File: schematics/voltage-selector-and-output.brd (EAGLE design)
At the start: 55.5 x 41.9 mm, 31 parts, among them IC1 5V, IC2 MIC2941, IC3 MCP41010P, IC5 12V, IC6 ATTINY85, Q1 2N3906

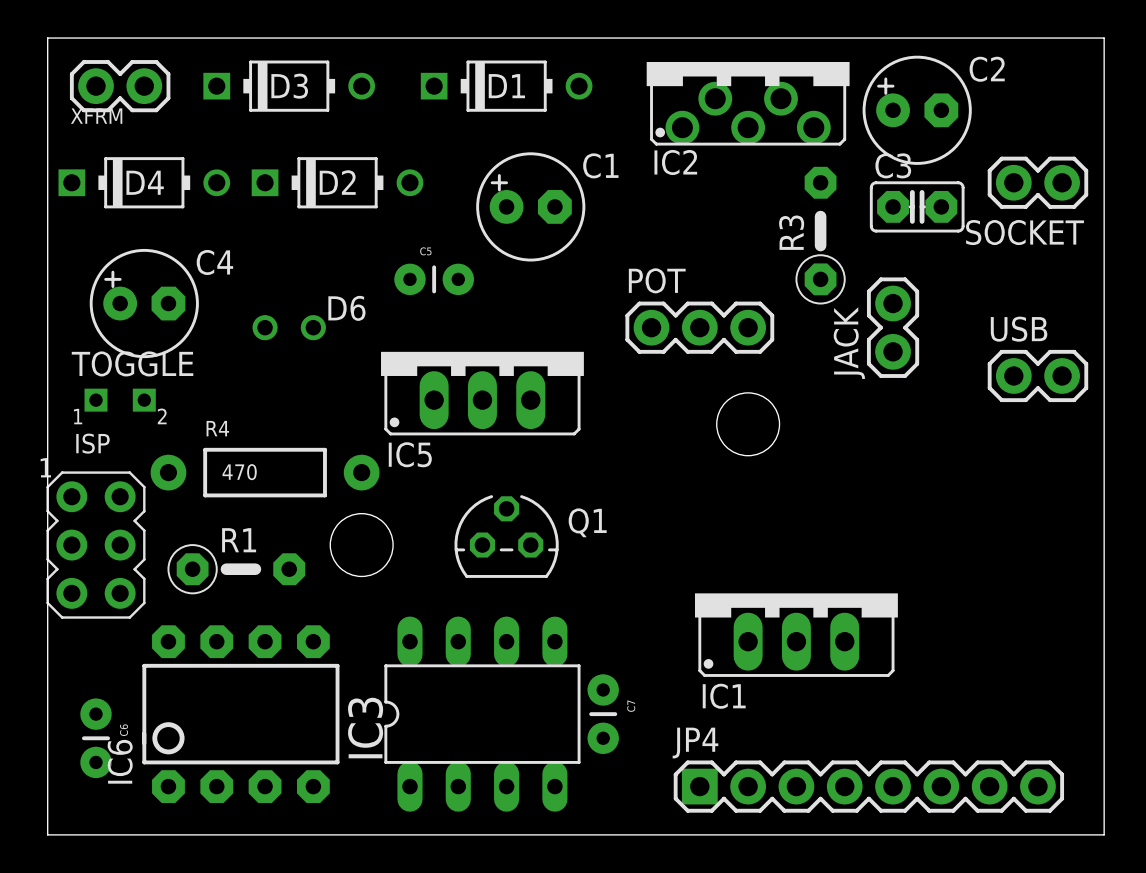
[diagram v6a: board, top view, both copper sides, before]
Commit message: Trying to deconflict the digi pot and register pins
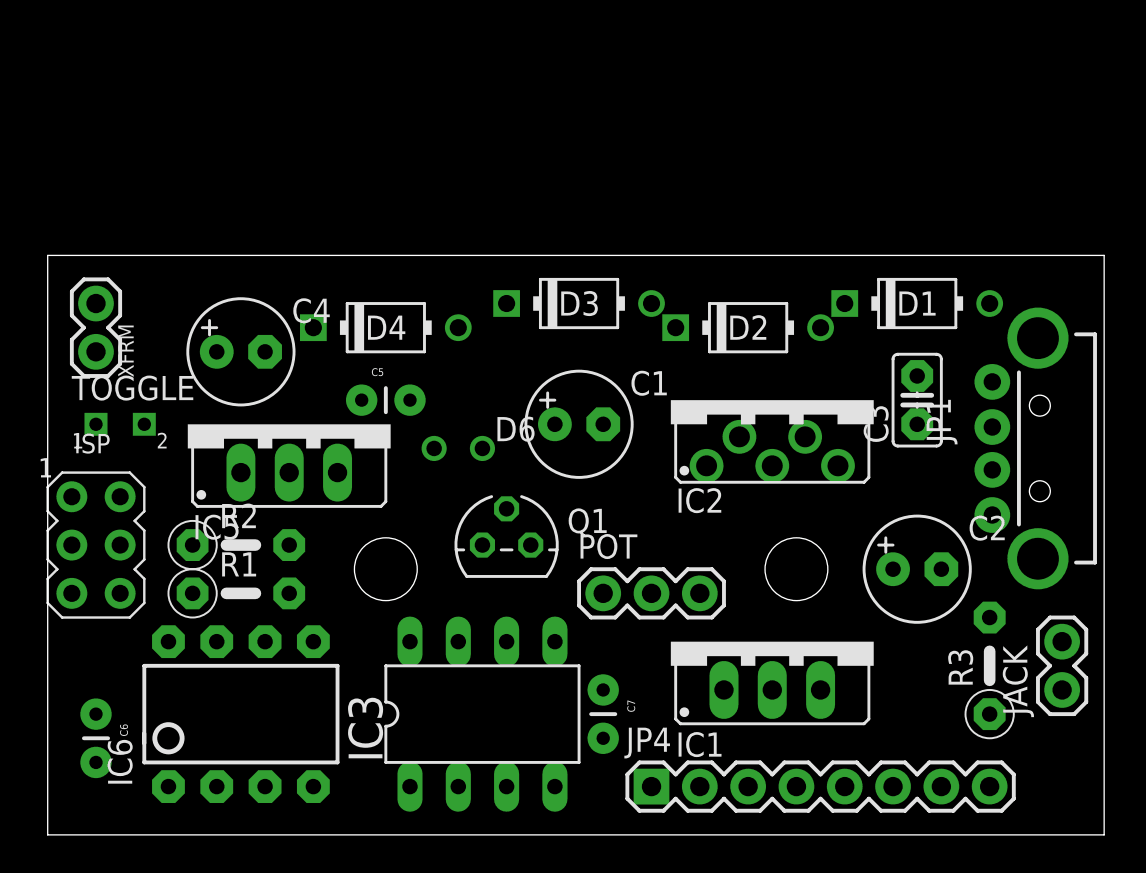
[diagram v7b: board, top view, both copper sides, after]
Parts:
- removed R4: 470, SparkFun-Resistors:AXIAL-0.4
- removed SOCKET, USB: (no value), SparkFun:1X02
- added JP1: USB-A-H, SparkFun-Connectors:USB-A-H
- added R2: 470, rcl-ez:0207/5V
- moved R3 24.5 mm to (49.5, 8.89)
- moved D1 24.4 mm to (45.7, 27.9)
- moved C2 24.1 mm to (45.7, 14.0)
- moved D2 22.9 mm to (36.8, 26.7)
- moved JACK 19.9 mm to (53.3, 7.62)
- moved D3 19.1 mm to (27.9, 27.9)
- moved IC2 17.8 mm to (38.1, 22.9)
- moved D4 14.8 mm to (17.8, 26.7)
- moved POT 14.2 mm to (29.2, 12.7)
- moved XFRM 14.0 mm to (2.54, 25.4), turned to 90 degrees
- moved C1 11.7 mm to (27.9, 21.6)
- moved D6 10.9 mm to (21.6, 20.3)
- moved IC5 10.9 mm to (12.7, 21.6)
- moved C3 10.2 mm to (45.7, 22.9), turned to 90 degrees
- moved STANDOFF2 8.03 mm to (39.4, 14.0)
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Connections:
- new net N$8: Q1.2
- net AGND: now also JP1.GND, R2.2; no longer R4.P$1, SOCKET.2, USB.2
- net N$5: now also R2.1; no longer R4.P$2
- net PB1: now also IC3.3
- net PB3: no longer IC3.1
- net PB5: now also IC3.1; no longer IC3.3
- net VADJ: now also JP1.VBUS; no longer SOCKET.1, USB.1
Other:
- board size 55.5 x 41.9 mm -> 55.5 x 30.5 mm

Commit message: LED was all wrong, of course
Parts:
- R2: value 470 -> 1k
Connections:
- new net N$10: D6.A, R2.2
- net AGND: no longer R2.2
- net N$5: now also C1.+, C5.1, IC5.OUT; no longer D6.K
- net RECTIFIED_12VCC: now also D6.K; no longer C1.+, C5.1, D6.A, IC5.OUT
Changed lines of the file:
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@@
 <attribute name="NAME" x="46.22" y="23.02" size="1.27" layer="25" rot="R270"/>
 </element>
-<element name="R2" library="rcl-ez" package="0207/5V" value="470" x="10.16" y="15.24"/>
+<element name="R2" library="rcl-ez" package="0207/5V" value="1k" x="10.16" y="15.24"/>
 </elements>
 <signals>
@@
 <contactref element="IC6" pad="4"/>
 <contactref element="ISP" pad="6"/>
-<contactref element="D4" pad="A"/>
-<contactref element="D3" pad="A"/>
-<contactref element="C4" pad="-"/>
 <contactref element="C1" pad="-"/>
-<contactref element="IC5" pad="GND"/>
 <contactref element="C5" pad="2"/>
 <contactref element="JACK" pad="2"/>
@@
 <contactref element="Q1" pad="3"/>
 <contactref element="JP1" pad="GND"/>
-<contactref element="R2" pad="2"/>
+<contactref element="D3" pad="A"/>
+<contactref element="D4" pad="A"/>
+<contactref element="C4" pad="-"/>
+<contactref element="IC5" pad="GND"/>
 <wire x1="49.67" y1="16.82" x2="45.72" y2="24.13" width="0" layer="19" extent="1-1"/>
 <wire x1="46.99" y1="13.97" x2="49.67" y2="16.82" width="0" layer="19" extent="1-1"/>
@@
 <wire x1="49.53" y1="6.35" x2="53.34" y2="10.16" width="0" layer="19" extent="1-1"/>
 <wire x1="49.53" y1="2.54" x2="49.53" y2="6.35" width="0" layer="19" extent="1-1"/>
-<wire x1="38.1" y1="7.62" x2="49.53" y2="6.35" width="0" layer="19" extent="1-1"/>
 <wire x1="38.1" y1="19.4056" x2="45.72" y2="24.13" width="0" layer="19" extent="1-1"/>
 <wire x1="36.3728" y1="20.9296" x2="38.1" y2="19.4056" width="0" layer="19" extent="1-1"/>
@@
 <wire x1="21.59" y1="26.67" x2="19.05" y2="22.86" width="0" layer="19" extent="1-1"/>
 <wire x1="12.7" y1="19.05" x2="19.05" y2="22.86" width="0" layer="19" extent="1-1"/>
-<wire x1="12.7" y1="15.24" x2="12.7" y2="19.05" width="0" layer="19" extent="1-1"/>
-<wire x1="7.62" y1="12.7" x2="12.7" y2="15.24" width="0" layer="19" extent="1-1"/>
+<wire x1="11.43" y1="25.4" x2="12.7" y2="19.05" width="0" layer="19" extent="1-1"/>
+<wire x1="7.62" y1="12.7" x2="12.7" y2="19.05" width="0" layer="19" extent="1-1"/>
 <wire x1="3.81" y1="12.7" x2="7.62" y2="12.7" width="0" layer="19" extent="1-1"/>
-<wire x1="11.43" y1="25.4" x2="12.7" y2="19.05" width="0" layer="19" extent="1-1"/>
 <wire x1="2.54" y1="3.81" x2="3.81" y2="12.7" width="0" layer="19" extent="1-1"/>
 <wire x1="29.21" y1="5.08" x2="21.59" y2="10.16" width="0" layer="19" extent="1-1"/>
 <wire x1="26.67" y1="2.54" x2="29.21" y2="5.08" width="0" layer="19" extent="1-1"/>
+<wire x1="38.1" y1="7.62" x2="29.21" y2="5.08" width="0" layer="19" extent="1-1"/>
 <wire x1="13.97" y1="2.54" x2="21.59" y2="10.16" width="0" layer="19" extent="1-1"/>
 </signal>
@@
 <contactref element="IC2" pad="4"/>
 <contactref element="IC1" pad="IN"/>
-<contactref element="C1" pad="+"/>
-<contactref element="IC5" pad="OUT"/>
-<contactref element="D6" pad="A"/>
-<contactref element="C5" pad="1"/>
-<wire x1="26.67" y1="21.59" x2="39.8272" y2="20.9296" width="0" layer="19" extent="1-1"/>
-<wire x1="20.32" y1="20.32" x2="26.67" y2="21.59" width="0" layer="19" extent="1-1"/>
-<wire x1="16.51" y1="22.86" x2="20.32" y2="20.32" width="0" layer="19" extent="1-1"/>
-<wire x1="15.24" y1="19.05" x2="16.51" y2="22.86" width="0" layer="19" extent="1-1"/>
+<contactref element="D6" pad="K"/>
 <wire x1="35.56" y1="7.62" x2="39.8272" y2="20.9296" width="0" layer="19" extent="1-1"/>
+<wire x1="22.86" y1="20.32" x2="39.8272" y2="20.9296" width="0" layer="19" extent="1-1"/>
 </signal>
 <signal name="N$2">
@@
 </signal>
 <signal name="N$5">
-<contactref element="D6" pad="K"/>
+<contactref element="IC5" pad="OUT"/>
+<contactref element="C5" pad="1"/>
 <contactref element="R2" pad="1"/>
-<wire x1="7.62" y1="15.24" x2="22.86" y2="20.32" width="0" layer="19" extent="1-1"/>
+<contactref element="C1" pad="+"/>
+<wire x1="16.51" y1="22.86" x2="26.67" y2="21.59" width="0" layer="19" extent="1-1"/>
+<wire x1="15.24" y1="19.05" x2="16.51" y2="22.86" width="0" layer="19" extent="1-1"/>
+<wire x1="7.62" y1="15.24" x2="15.24" y2="19.05" width="0" layer="19" extent="1-1"/>
+</signal>
+<signal name="N$10">
+<contactref element="R2" pad="2"/>
+<contactref element="D6" pad="A"/>
+<wire x1="12.7" y1="15.24" x2="20.32" y2="20.32" width="0" layer="19" extent="1-1"/>
 </signal>
 </signals>
